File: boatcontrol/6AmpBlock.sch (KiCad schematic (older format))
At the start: 15 parts, among them U7901 ULN2803A

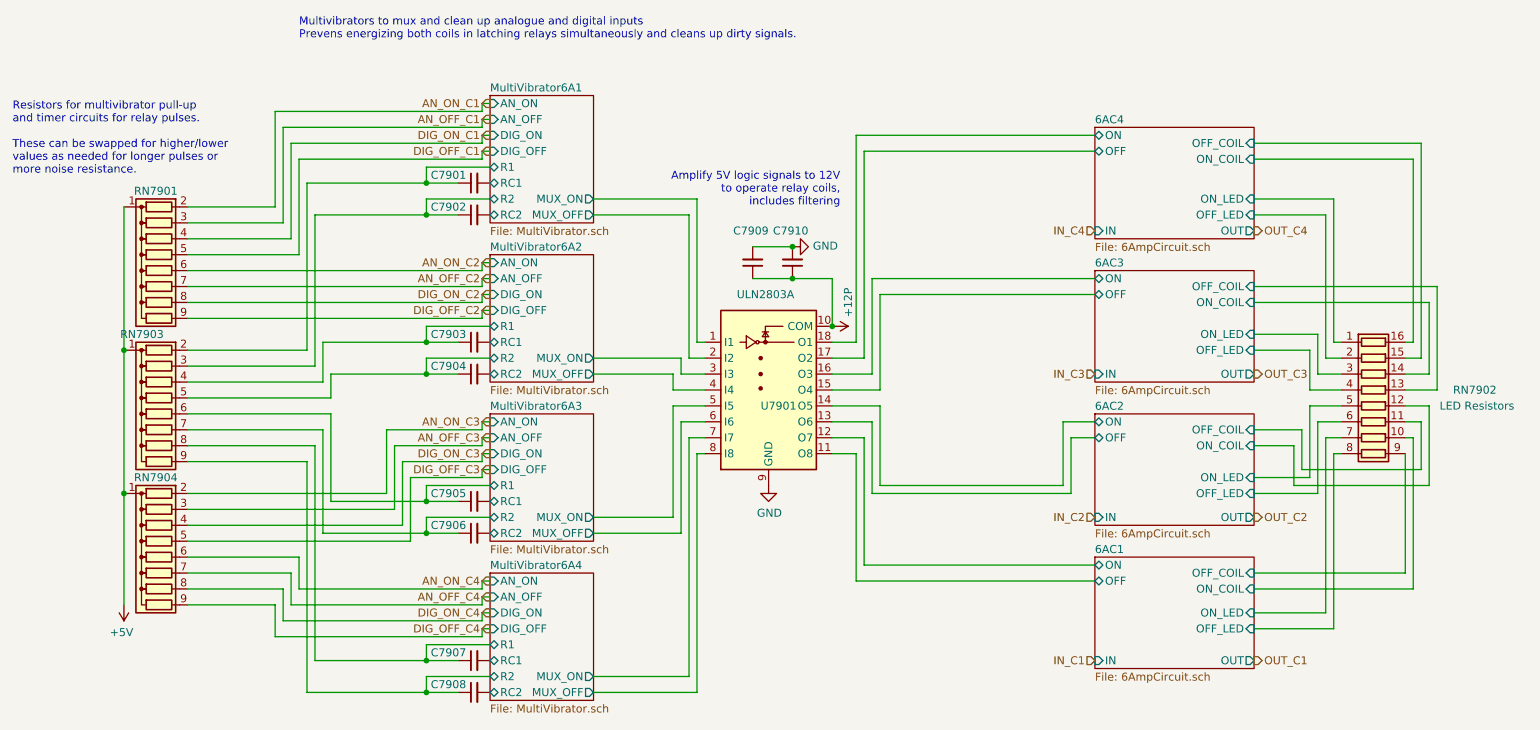
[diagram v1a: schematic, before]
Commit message: Fix resistor network values
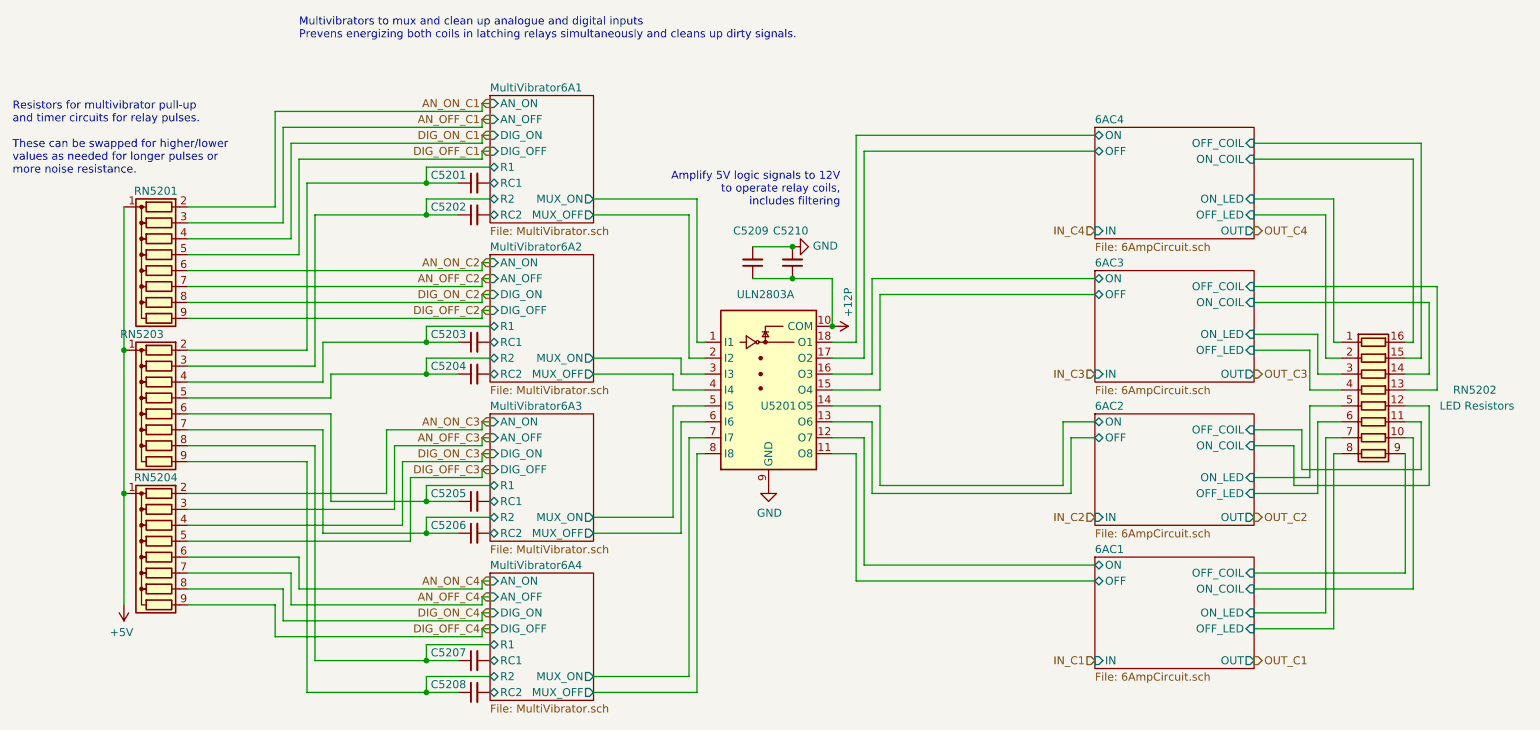
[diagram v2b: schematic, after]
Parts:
- RN7901, RN7904: value 100K Ohm -> 100KΩ
- RN7903: value 10M Ohm -> 10MΩ
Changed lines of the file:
@@
 $Descr A4 11693 8268
 encoding utf-8
-Sheet 89 97
+Sheet 62 97
 Title "Boat Control Hat"
 Date "2020-07-09"
@@
 AR Path="/D1BB8DB4/5F317CB5/60365AE4" Ref="#PWR07901"  Part="1"
 AR Path="/D1BB8DB4/5F746103/60365AE4" Ref="#PWR05201"  Part="1"
-F 0 "#PWR07901" H 6700 3400 50  0001 C CNN
+F 0 "#PWR05201" H 6700 3400 50  0001 C CNN
 F 1 "+12P" H 6550 3650 50  0000 C CNN
 F 2 "" H 6700 3550 50  0001 C CNN
@@
 AR Path="/D1BB8DB4/5F317CB5/60365AF1" Ref="U7901"  Part="1"
 AR Path="/D1BB8DB4/5F746103/60365AF1" Ref="U5201"  Part="1"
-F 0 "U7901" H 6250 3650 50  0000 L CNN
+F 0 "U5201" H 6250 3650 50  0000 L CNN
 F 1 "ULN2803A" H 6100 4350 50  0000 L CNN
 F 2 "Package_DIP:DIP-18_W7.62mm" H 6350 3200 50  0001 L CNN
@@
 AR Path="/D1BB8DB4/5F317CB5/60365B03" Ref="#PWR07902"  Part="1"
 AR Path="/D1BB8DB4/5F746103/60365B03" Ref="#PWR05202"  Part="1"
-F 0 "#PWR07902" H 6300 4300 50  0001 C CNN
+F 0 "#PWR05202" H 6300 4300 50  0001 C CNN
 F 1 "GND" H 6305 4377 50  0000 C CNN
 F 2 "" H 6300 4550 50  0001 C CNN
@@
 AR Path="/D1BB8DB4/5F317CB5/60365B8C" Ref="#PWR07903"  Part="1"
 AR Path="/D1BB8DB4/5F746103/60365B8C" Ref="#PWR05203"  Part="1"
-F 0 "#PWR07903" H 2250 5150 50  0001 C CNN
+F 0 "#PWR05203" H 2250 5150 50  0001 C CNN
 F 1 "+5V" H 2265 5473 50  0000 C CNN
 F 2 "" H 2250 5300 50  0001 C CNN
@@
 AR Path="/D1BB8DB4/5F317CB5/60365C68" Ref="RN7902"  Part="1"
 AR Path="/D1BB8DB4/5F746103/60365C68" Ref="RN5202"  Part="1"
-F 0 "RN7902" V 10000 4550 50  0000 L CNN
+F 0 "RN5202" V 10000 4550 50  0000 L CNN
 F 1 "680Ω" V 9600 3900 50  0001 L CNN
 F 2 "BoatControl:DIP254P762X432-16P" V 10575 4050 50  0001 C CNN
@@
 AR Path="/D1BB8DB4/5F746103/62AB509B" Ref="C5201"  Part="1"
 AR Path="/D1BB8DB4/5F317CB5/62AB509B" Ref="C7901"  Part="1"
-F 0 "C7901" V 4400 2700 50  0000 L CNN
+F 0 "C5201" V 4400 2700 50  0000 L CNN
 F 1 "1µF" H 3600 2550 50  0001 L CNN
 F 2 "Capacitor_THT:C_Disc_D7.5mm_W5.0mm_P5.00mm" H 4450 2650 50  0001 C CNN
@@
 AR Path="/D1BB8DB4/5F746103/62AC1E93" Ref="C5202"  Part="1"
 AR Path="/D1BB8DB4/5F317CB5/62AC1E93" Ref="C7902"  Part="1"
-F 0 "C7902" V 4400 2900 50  0000 L CNN
+F 0 "C5202" V 4400 2900 50  0000 L CNN
 F 1 "1µF" H 3600 2750 50  0001 L CNN
 F 2 "Capacitor_THT:C_Disc_D7.5mm_W5.0mm_P5.00mm" H 4450 2850 50  0001 C CNN
@@
 AR Path="/D1BB8DB4/5F746103/62ADD9A6" Ref="C5208"  Part="1"
 AR Path="/D1BB8DB4/5F317CB5/62ADD9A6" Ref="C7908"  Part="1"
-F 0 "C7908" V 4400 5900 50  0000 L CNN
+F 0 "C5208" V 4400 5900 50  0000 L CNN
 F 1 "1µF" H 3600 5750 50  0001 L CNN
 F 2 "Capacitor_THT:C_Disc_D7.5mm_W5.0mm_P5.00mm" H 4450 5850 50  0001 C CNN
@@
 AR Path="/D1BB8DB4/5F746103/62AEACF8" Ref="C5207"  Part="1"
 AR Path="/D1BB8DB4/5F317CB5/62AEACF8" Ref="C7907"  Part="1"
-F 0 "C7907" V 4400 5700 50  0000 L CNN
+F 0 "C5207" V 4400 5700 50  0000 L CNN
 F 1 "1µF" H 3600 5550 50  0001 L CNN
 F 2 "Capacitor_THT:C_Disc_D7.5mm_W5.0mm_P5.00mm" H 4450 5650 50  0001 C CNN
@@
 AR Path="/D1BB8DB4/5F746103/62AF81A3" Ref="C5206"  Part="1"
 AR Path="/D1BB8DB4/5F317CB5/62AF81A3" Ref="C7906"  Part="1"
-F 0 "C7906" V 4400 4900 50  0000 L CNN
+F 0 "C5206" V 4400 4900 50  0000 L CNN
 F 1 "1µF" H 3600 4750 50  0001 L CNN
 F 2 "Capacitor_THT:C_Disc_D7.5mm_W5.0mm_P5.00mm" H 4450 4850 50  0001 C CNN
@@
 AR Path="/D1BB8DB4/5F746103/62B05762" Ref="C5205"  Part="1"
 AR Path="/D1BB8DB4/5F317CB5/62B05762" Ref="C7905"  Part="1"
-F 0 "C7905" V 4400 4700 50  0000 L CNN
+F 0 "C5205" V 4400 4700 50  0000 L CNN
 F 1 "1µF" H 3600 4550 50  0001 L CNN
 F 2 "Capacitor_THT:C_Disc_D7.5mm_W5.0mm_P5.00mm" H 4450 4650 50  0001 C CNN
@@
 AR Path="/D1BB8DB4/5F746103/62B3C5BA" Ref="C5203"  Part="1"
 AR Path="/D1BB8DB4/5F317CB5/62B3C5BA" Ref="C7903"  Part="1"
-F 0 "C7903" V 4400 3700 50  0000 L CNN
+F 0 "C5203" V 4400 3700 50  0000 L CNN
 F 1 "1µF" H 3600 3550 50  0001 L CNN
 F 2 "Capacitor_THT:C_Disc_D7.5mm_W5.0mm_P5.00mm" H 4450 3650 50  0001 C CNN
@@
 AR Path="/D1BB8DB4/5F746103/62B4996D" Ref="C5204"  Part="1"
 AR Path="/D1BB8DB4/5F317CB5/62B4996D" Ref="C7904"  Part="1"
-F 0 "C7904" V 4400 3900 50  0000 L CNN
+F 0 "C5204" V 4400 3900 50  0000 L CNN
 F 1 "1µF" H 3600 3750 50  0001 L CNN
 F 2 "Capacitor_THT:C_Disc_D7.5mm_W5.0mm_P5.00mm" H 4450 3850 50  0001 C CNN
@@
 AR Path="/D1BB8DB4/5F317CB5/62C7A7CE" Ref="RN7903"  Part="1"
 AR Path="/D1BB8DB4/5F746103/62C7A7CE" Ref="RN5203"  Part="1"
-F 0 "RN7903" V 1950 4050 50  0000 L CNN
-F 1 "10M Ohm" H 2100 3700 50  0001 L CNN
+F 0 "RN5203" V 1950 4050 50  0000 L CNN
+F 1 "10MΩ" H 2100 3700 50  0001 L CNN
 F 2 "Resistor_THT:R_Array_SIP9" V 2925 4100 50  0001 C CNN
 F 3 "https://www.bourns.com/docs/Product-Datasheets/4600x.pdf" H 2450 4100 50  0001 C CNN
@@
 AR Path="/D1BB8DB4/5F317CB5/62F1D24C" Ref="RN7904"  Part="1"
 AR Path="/D1BB8DB4/5F746103/62F1D24C" Ref="RN5204"  Part="1"
-F 0 "RN7904" V 1950 5000 50  0000 C CNN
-F 1 "100K Ohm" V 2250 4700 50  0001 C CNN
+F 0 "RN5204" V 1950 5000 50  0000 C CNN
+F 1 "100KΩ" V 2250 4700 50  0001 C CNN
 F 2 "Resistor_THT:R_Array_SIP9" H 3200 5100 50  0001 L CNN
 F 3 "http://www.bourns.com/pdfs/4100R.pdf" H 3200 5000 50  0001 L CNN
@@
 AR Path="/D1BB8DB4/5F317CB5/62F2A731" Ref="RN7901"  Part="1"
 AR Path="/D1BB8DB4/5F746103/62F2A731" Ref="RN5201"  Part="1"
-F 0 "RN7901" V 1950 3200 50  0000 C CNN
-F 1 "100K Ohm" V 2250 2900 50  0001 C CNN
+F 0 "RN5201" V 1950 3200 50  0000 C CNN
+F 1 "100KΩ" V 2250 2900 50  0001 C CNN
 F 2 "Resistor_THT:R_Array_SIP9" H 3200 3300 50  0001 L CNN
 F 3 "http://www.bourns.com/pdfs/4100R.pdf" H 3200 3200 50  0001 L CNN
@@
 AR Path="/D1BB8DB4/5F317CB5/624D8B2F" Ref="C7909"  Part="1"
 AR Path="/D1BB8DB4/5F746103/624D8B2F" Ref="C5209"  Part="1"
-F 0 "C7909" H 6100 2950 50  0000 L CNN
+F 0 "C5209" H 6100 2950 50  0000 L CNN
 F 1 "10uF" H 6291 3105 50  0001 L CNN
 F 2 "Capacitor_THT:C_Disc_D7.5mm_W5.0mm_P5.00mm" H 6200 3150 50  0001 C CNN
@@
 AR Path="/D1BB8DB4/5F317CB5/624D8B37" Ref="C7910"  Part="1"
 AR Path="/D1BB8DB4/5F746103/624D8B37" Ref="C5210"  Part="1"
-F 0 "C7910" H 6350 2950 50  0000 L CNN
+F 0 "C5210" H 6350 2950 50  0000 L CNN
 F 1 "0.1uF" H 6541 3105 50  0001 L CNN
 F 2 "Capacitor_THT:C_Disc_D7.5mm_W5.0mm_P5.00mm" H 6450 3150 50  0001 C CNN
@@
 AR Path="/D1BB8DB4/5F317CB5/624D8B3E" Ref="#PWR0204"  Part="1"
 AR Path="/D1BB8DB4/5F746103/624D8B3E" Ref="#PWR0198"  Part="1"
-F 0 "#PWR0204" H 6450 2800 50  0001 C CNN
+F 0 "#PWR0198" H 6450 2800 50  0001 C CNN
 F 1 "GND" V 6455 2922 50  0000 R CNN
 F 2 "" H 6450 3050 50  0001 C CNN

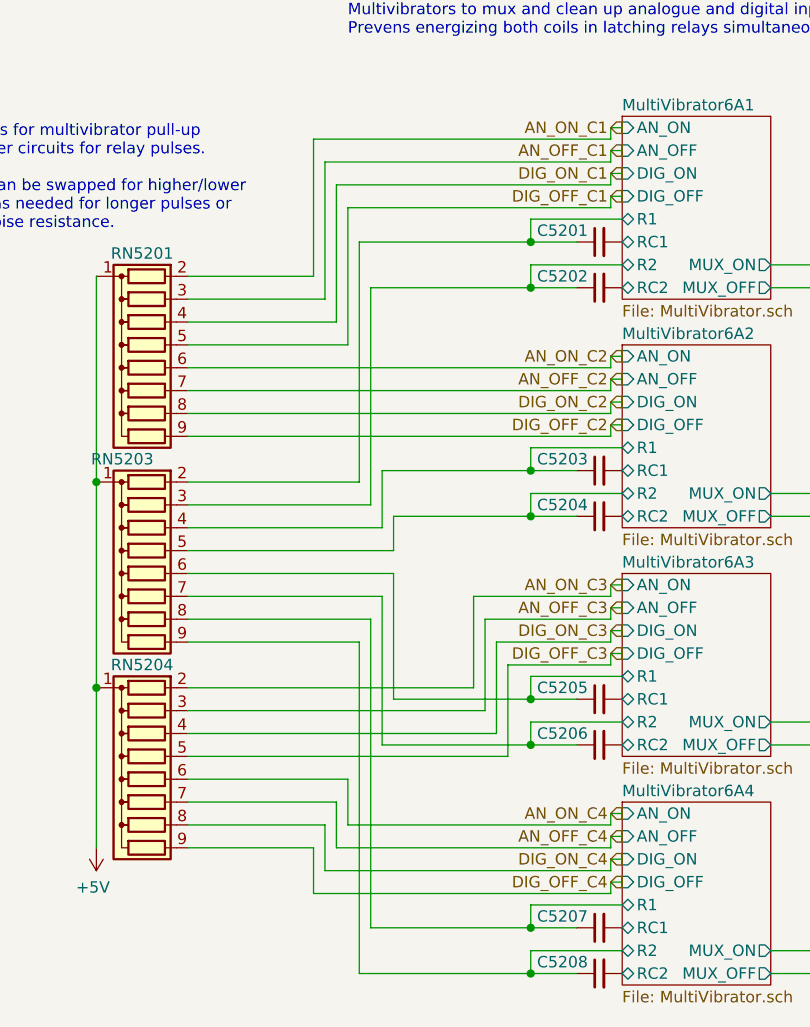
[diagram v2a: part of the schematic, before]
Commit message: Rewiring resistors done
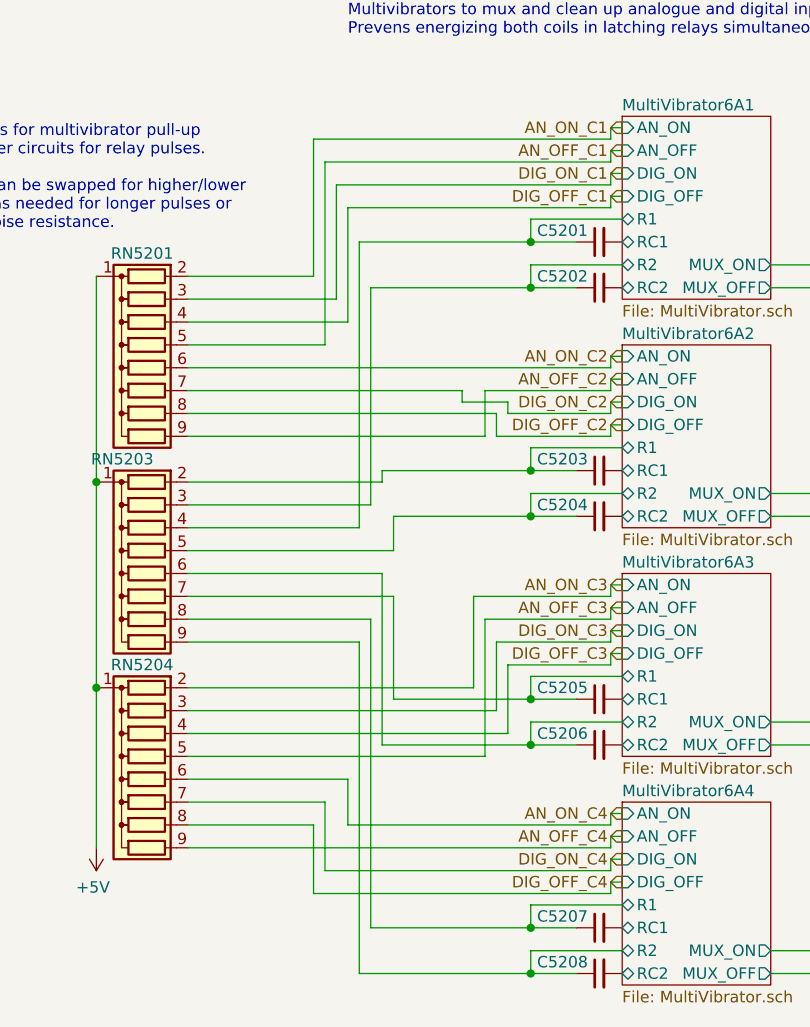
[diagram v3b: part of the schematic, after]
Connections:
- net AN_OFF_C1: now also RN7901.5 (R4); no longer RN7901.3 (R2)
- net AN_OFF_C2: now also RN7901.9 (R8); no longer RN7901.7 (R6)
- net AN_OFF_C3: now also RN7904.5 (R4); no longer RN7904.3 (R2)
- net AN_OFF_C4: now also RN7904.9 (R8); no longer RN7904.7 (R6)
- net DIG_OFF_C1: now also RN7901.4 (R3); no longer RN7901.5 (R4)
- net DIG_OFF_C2: now also RN7901.8 (R7); no longer RN7901.9 (R8)
- net DIG_OFF_C3: now also RN7904.4 (R3); no longer RN7904.5 (R4)
- net DIG_OFF_C4: now also RN7904.8 (R7); no longer RN7904.9 (R8)
- net DIG_ON_C1: now also RN7901.3 (R2); no longer RN7901.4 (R3)
- net DIG_ON_C2: now also RN7901.7 (R6); no longer RN7901.8 (R7)
- net DIG_ON_C3: now also RN7904.3 (R2); no longer RN7904.4 (R3)
- net DIG_ON_C4: now also RN7904.7 (R6); no longer RN7904.8 (R7)
- net MultiVibrator6A1/R1: now also RN7903.4 (R3); no longer RN7903.2 (R1)
- net MultiVibrator6A2/R1: now also RN7903.2 (R1); no longer RN7903.4 (R3)
- net MultiVibrator6A3/R1: now also RN7903.7 (R6); no longer RN7903.6 (R5)
- net MultiVibrator6A3/R2: now also RN7903.6 (R5); no longer RN7903.7 (R6)
